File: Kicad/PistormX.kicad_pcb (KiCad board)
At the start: 2 copper layers, 82.6 x 34.3 mm, 19 parts, among them J1 68000D socket, J2 Raspberry_Pi_2_3, J3 PROG, U1 XC95144XL-TQ100, U2 SPX3819M5-L-3-3, U3 XC6206PxxxMR

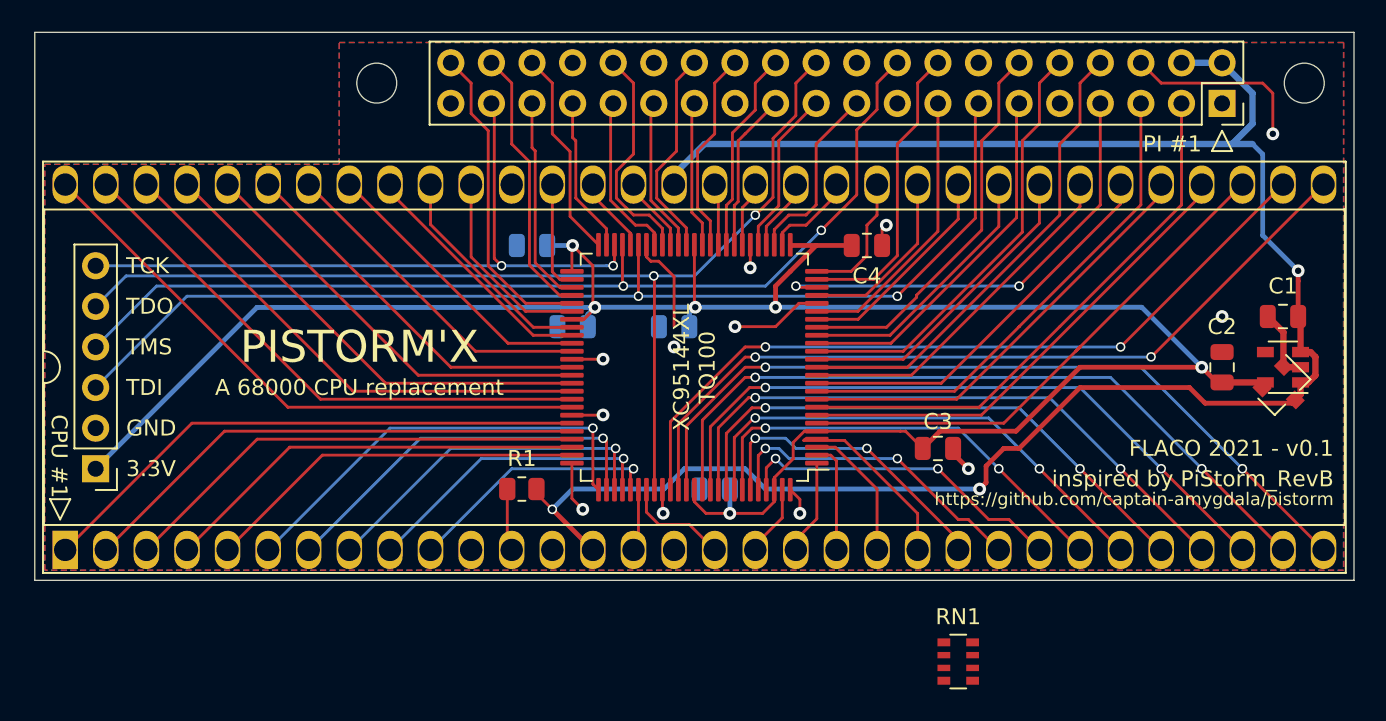
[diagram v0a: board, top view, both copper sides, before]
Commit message: Kicad : first board revision ; CPLD : working with buptest and emulator, no 200MHz PICLK is used, fixed cold and warm reset
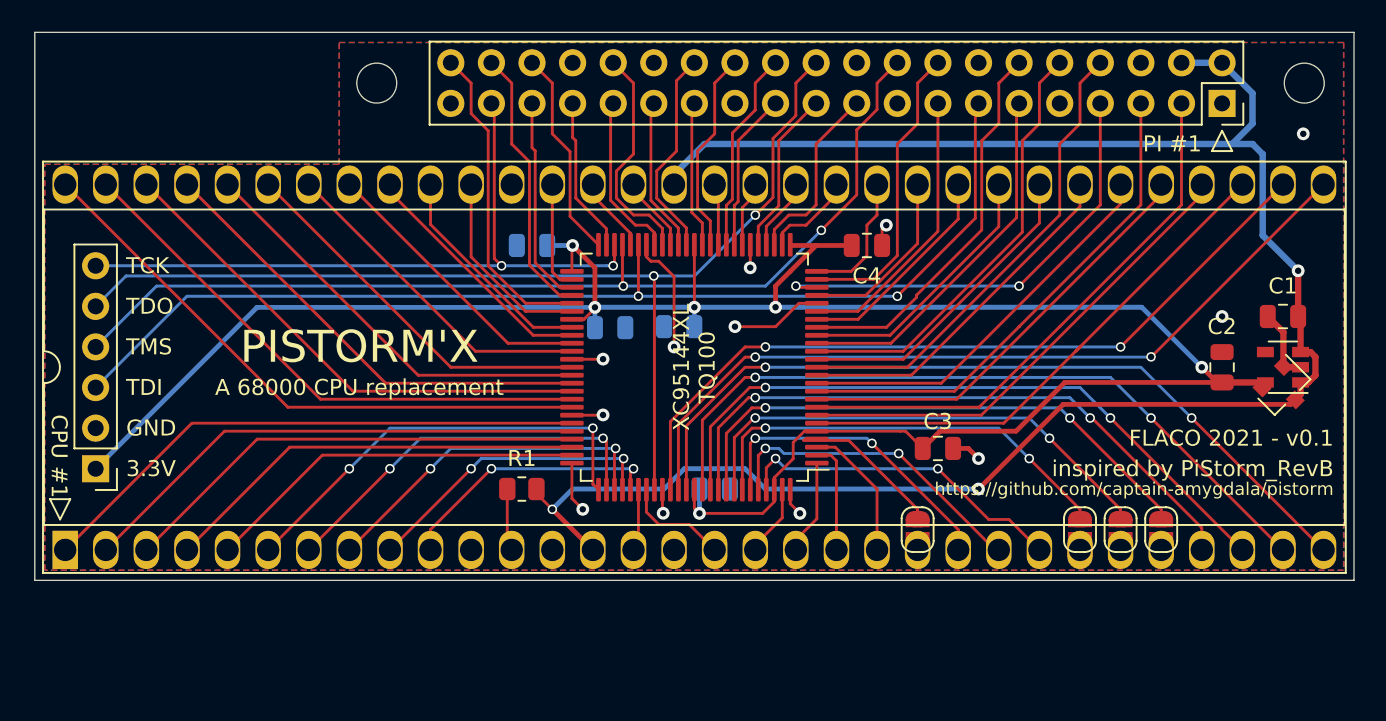
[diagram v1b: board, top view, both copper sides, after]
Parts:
- removed RN1: 10k, Resistor_SMD:R_Array_Convex_4x0603
- added JP2: BERR, Jumper:SolderJumper-2_P1.3mm_Open_RoundedPad1.0x1.5mm, F.Cu at (223.5, 123.2)
- added JP3: BERR, Jumper:SolderJumper-2_P1.3mm_Open_RoundedPad1.0x1.5mm, F.Cu at (221.0, 123.2)
- added JP4: BERR, Jumper:SolderJumper-2_P1.3mm_Open_RoundedPad1.0x1.5mm, F.Cu at (218.4, 123.2)
- added JP5: BERR, Jumper:SolderJumper-2_P1.3mm_Open_RoundedPad1.0x1.5mm, F.Cu at (208.3, 123.2)
- moved FID1 6.25 mm to (194.9, 111.8), turned to 0 degrees
- moved C8 2.35 mm to (189.0, 110.6), turned to 0 degrees
- moved C7 0.32 mm to (193.4, 110.5)
- turned C6 to 0 degrees
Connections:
- U1 pad 4: /BERR -> /BERR-
- U1 pad 92: /FC0 -> /FC0-
- U1 pad 93: /FC1 -> /FC1-
- U1 pad 94: /FC2 -> /FC2-
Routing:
- net /FC0: track 35.1 -> 0.00 mm, vias 2 -> 0
- net /FC0-: track 0.00 -> 34.6 mm, vias 0 -> 2
- net /FC1: track 31.4 -> 0.00 mm, vias 2 -> 0
- net /FC1-: track 0.00 -> 30.9 mm, vias 0 -> 2
- net /FC2: track 27.8 -> 0.00 mm, vias 2 -> 0
- net /FC2-: track 0.00 -> 27.4 mm, vias 0 -> 2
- net /BERR: track 12.1 -> 0.00 mm
- net /BERR-: track 0.00 -> 10.4 mm
- net GND: track 42.9 -> 32.7 mm
- net +5V: track 122.4 -> 121.0 mm
- net +3V3: track 145.1 -> 146.0 mm
- net /A1: track 38.8 -> 39.7 mm
- net /_DTACK: track 16.2 -> 16.9 mm, vias 1 -> 2
- net /_UDS: vias 1 -> 2
- net /_LDS: vias 1 -> 2
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
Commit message: Kicad: converted to v6, relabeled the Pi signals in schematic, added EXPERIMENTAL and CC-BY-NC-SA on silkscreen ; CPLD: add JED files ; Photo
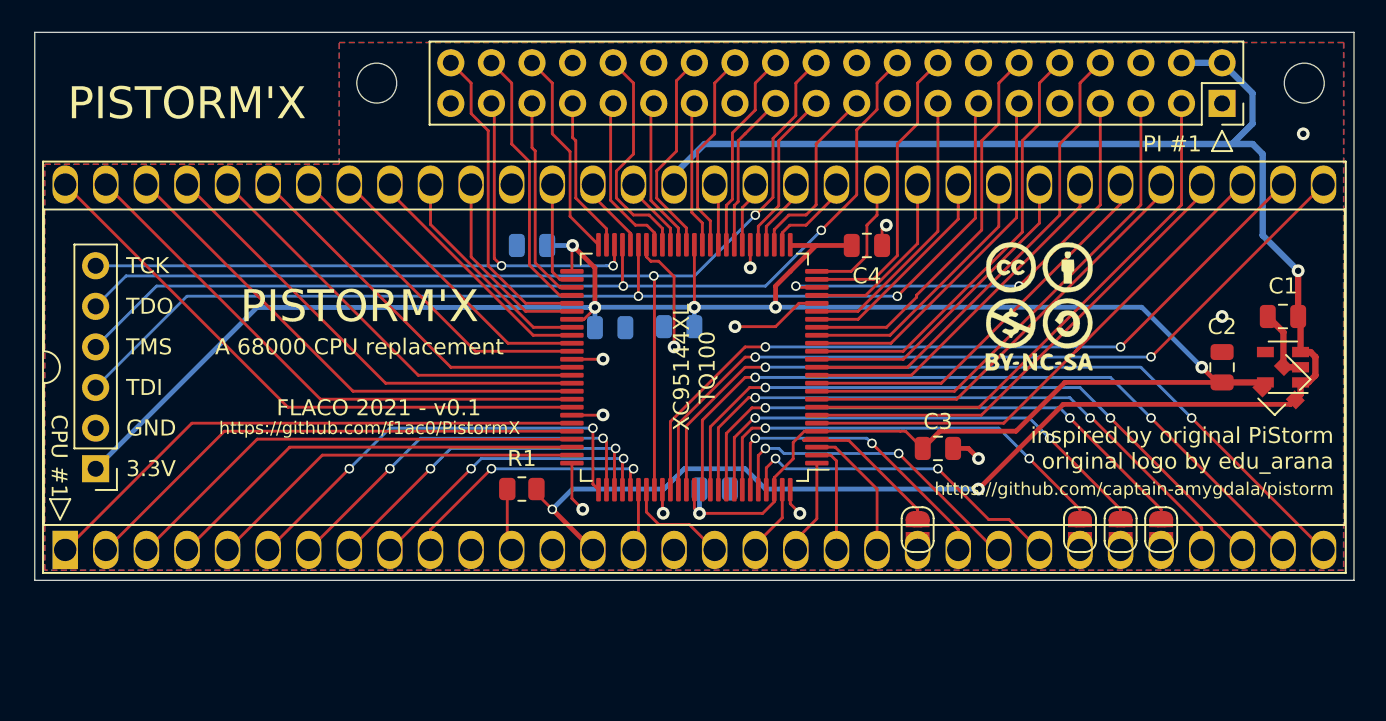
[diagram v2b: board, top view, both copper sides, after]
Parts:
- added FID2: License, Sassa:CC_BY_NC_SA_square_silkscreen, F.Cu at (215.9, 109.2)
- JP2: value BERR -> FC0
- JP3: value BERR -> FC1
- JP4: value BERR -> FC2
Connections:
- net /AUX0 renamed /PI_TXN_IN_PROCESS
- net /AUX1 renamed /PI_IPL_0
- net /PICLK renamed /PI_CLK
- net /SA0 renamed /PI_RESET
- net /SA1 renamed /PI_A1
- net /SA2 renamed /PI_A0
- net /SOE renamed /PI_RD
- net /SWE renamed /PI_WR
- J1 pad 11: Net-(J1-Pad11) -> unconnected-(J1-Pad11)
- J1 pad 13: Net-(J1-Pad13) -> unconnected-(J1-Pad13)
- U2 pad 4: Net-(U2-Pad4) -> unconnected-(U2-Pad4)
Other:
- net class Default removed
- net class Mid removed
- net class Power removed
- board text added: "EXPERIMENTAL DO NOT SELL OR BUY"
- board text added: "https://github.com/f1ac0/PistormX"
- board text added: "inspired by original PiStorm original logo by edu_arana"
- board text removed: "inspired by PiStorm_RevB"
